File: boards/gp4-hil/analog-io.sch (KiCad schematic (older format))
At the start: 155 parts, among them U10 AD9609, U11 DAC084S085, U12 DAC084S085, U13 DAC084S085, U14 DAC084S085, U19 TS3A4751, U2 XC7A100T-1FTG256C, U25 TS3A4751, U26 TS3A4751, U27 TS3A4751, U28 TS3A4751, U31 ADA4937-2, U34 INA199A2RSW, U35 INA199A2RSW, U36 INA199A2RSW, U8 ADG726, U9 AD9609

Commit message: Began work on footprint creation for layout.
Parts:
- C145, C146, C147, C148, C149, C150, C151, C152, C153, C154, C155, C156, C157, C158, C159, C160, C161, C162, C167, C168, C176, C177, C178, C184, C185, C27, C28, C36, C37, C38, C39, C42, C43, C44, C45, C50, C51, C52, C53: footprint (none) -> azonenberg_pcb:EIA_0402_CAP_NOSILK
- C169, C170, C26, C30, C32, C34, C35, C40, C41, C46, C47, C48, C49, C55: footprint (none) -> azonenberg_pcb:EIA_0603_CAP_NOSILK
- C25, C29, C31, C33, C54, C56: footprint (none) -> azonenberg_pcb:EIA_1206_CAP_NOSILK
- L3, L4, L5: footprint (none) -> azonenberg_pcb:EIA_0805_INDUCTOR_NOSILK

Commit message: Updated PCB with a lot more component footprints
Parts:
- L3, L4, L5: footprint azonenberg_pcb:EIA_0805_INDUCTOR_NOSILK -> azonenberg_pcb:EIA_0603_INDUCTOR_NOSILK
- R138, R139, R140, R141, R59, R60, R61, R62, R63, R64, R65, R66, R67, R68, R69, R70, R71, R72, R73, R74, R75, R76, R77, R78, R79, R80: footprint (none) -> azonenberg_pcb:EIA_0402_RES_NOSILK
- U2: footprint (none) -> azonenberg_pcb:BGA_256_17x17_FULLARRAY_1MM
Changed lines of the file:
@@
 Sheet 5 7
 Title "GreenPak Hardware-In-Loop Test Platform"
-Date "2016-05-19"
+Date "2016-05-20"
 Rev "0.1"
 Comp "Andrew Zonenberg"
@@
 F 0 "U2" H 20850 5850 60  0000 L CNN
 F 1 "XC7A100T-1FTG256C" H 20850 5950 60  0000 L CNN
-F 2 "" H 20850 6050 60  0001 C CNN
+F 2 "azonenberg_pcb:BGA_256_17x17_FULLARRAY_1MM" H 20850 6050 60  0001 C CNN
 F 3 "" H 20850 6050 60  0000 C CNN
 	4    20850 6050
@@
 F 0 "L3" V 8742 750 40  0000 C CNN
 F 1 "600R" V 8820 750 40  0000 C CNN
-F 2 "azonenberg_pcb:EIA_0805_INDUCTOR_NOSILK" H 8900 750 60  0001 C CNN
+F 2 "azonenberg_pcb:EIA_0603_INDUCTOR_NOSILK" H 8900 750 60  0001 C CNN
 F 3 "" H 8900 750 60  0000 C CNN
 	1    8900 750
@@
 F 0 "R60" V 3350 8900 50  0000 C CNN
 F 1 "33" V 3400 8700 50  0000 C CNN
-F 2 "" V 3330 8700 30  0001 C CNN
+F 2 "azonenberg_pcb:EIA_0402_RES_NOSILK" V 3330 8700 30  0001 C CNN
 F 3 "" H 3400 8700 30  0000 C CNN
 	1    3400 8700
@@
 F 0 "R61" V 3350 9000 50  0000 C CNN
 F 1 "33" V 3400 8800 50  0000 C CNN
-F 2 "" V 3330 8800 30  0001 C CNN
+F 2 "azonenberg_pcb:EIA_0402_RES_NOSILK" V 3330 8800 30  0001 C CNN
 F 3 "" H 3400 8800 30  0000 C CNN
 	1    3400 8800
@@
 F 0 "R62" V 3350 9100 50  0000 C CNN
 F 1 "33" V 3400 8900 50  0000 C CNN
-F 2 "" V 3330 8900 30  0001 C CNN
+F 2 "azonenberg_pcb:EIA_0402_RES_NOSILK" V 3330 8900 30  0001 C CNN
 F 3 "" H 3400 8900 30  0000 C CNN
 	1    3400 8900
@@
 F 0 "R63" V 3350 9200 50  0000 C CNN
 F 1 "33" V 3400 9000 50  0000 C CNN
-F 2 "" V 3330 9000 30  0001 C CNN
+F 2 "azonenberg_pcb:EIA_0402_RES_NOSILK" V 3330 9000 30  0001 C CNN
 F 3 "" H 3400 9000 30  0000 C CNN
 	1    3400 9000
@@
 F 0 "R64" V 3350 9300 50  0000 C CNN
 F 1 "33" V 3400 9100 50  0000 C CNN
-F 2 "" V 3330 9100 30  0001 C CNN
+F 2 "azonenberg_pcb:EIA_0402_RES_NOSILK" V 3330 9100 30  0001 C CNN
 F 3 "" H 3400 9100 30  0000 C CNN
 	1    3400 9100
@@
 F 0 "R65" V 3350 9400 50  0000 C CNN
 F 1 "33" V 3400 9200 50  0000 C CNN
-F 2 "" V 3330 9200 30  0001 C CNN
+F 2 "azonenberg_pcb:EIA_0402_RES_NOSILK" V 3330 9200 30  0001 C CNN
 F 3 "" H 3400 9200 30  0000 C CNN
 	1    3400 9200
@@
 F 0 "R66" V 3350 9500 50  0000 C CNN
 F 1 "33" V 3400 9300 50  0000 C CNN
-F 2 "" V 3330 9300 30  0001 C CNN
+F 2 "azonenberg_pcb:EIA_0402_RES_NOSILK" V 3330 9300 30  0001 C CNN
 F 3 "" H 3400 9300 30  0000 C CNN
 	1    3400 9300
@@
 F 0 "R67" V 3350 9600 50  0000 C CNN
 F 1 "33" V 3400 9400 50  0000 C CNN
-F 2 "" V 3330 9400 30  0001 C CNN
+F 2 "azonenberg_pcb:EIA_0402_RES_NOSILK" V 3330 9400 30  0001 C CNN
 F 3 "" H 3400 9400 30  0000 C CNN
 	1    3400 9400
@@
 F 0 "R68" V 3350 9700 50  0000 C CNN
 F 1 "33" V 3400 9500 50  0000 C CNN
-F 2 "" V 3330 9500 30  0001 C CNN
+F 2 "azonenberg_pcb:EIA_0402_RES_NOSILK" V 3330 9500 30  0001 C CNN
 F 3 "" H 3400 9500 30  0000 C CNN
 	1    3400 9500
@@
 F 0 "R69" V 3350 9800 50  0000 C CNN
 F 1 "33" V 3400 9600 50  0000 C CNN
-F 2 "" V 3330 9600 30  0001 C CNN
+F 2 "azonenberg_pcb:EIA_0402_RES_NOSILK" V 3330 9600 30  0001 C CNN
 F 3 "" H 3400 9600 30  0000 C CNN
 	1    3400 9600
@@
 F 0 "R59" V 3350 8700 50  0000 C CNN
 F 1 "33" V 3400 8500 50  0000 C CNN
-F 2 "" V 3330 8500 30  0001 C CNN
+F 2 "azonenberg_pcb:EIA_0402_RES_NOSILK" V 3330 8500 30  0001 C CNN
 F 3 "" H 3400 8500 30  0000 C CNN
 	1    3400 8500
@@
 F 0 "L4" V 6342 750 40  0000 C CNN
 F 1 "600R" V 6420 750 40  0000 C CNN
-F 2 "azonenberg_pcb:EIA_0805_INDUCTOR_NOSILK" H 6500 750 60  0001 C CNN
+F 2 "azonenberg_pcb:EIA_0603_INDUCTOR_NOSILK" H 6500 750 60  0001 C CNN
 F 3 "" H 6500 750 60  0000 C CNN
 	1    6500 750
@@
 F 0 "R71" V 3350 12750 50  0000 C CNN
 F 1 "33" V 3400 12550 50  0000 C CNN
-F 2 "" V 3330 12550 30  0001 C CNN
+F 2 "azonenberg_pcb:EIA_0402_RES_NOSILK" V 3330 12550 30  0001 C CNN
 F 3 "" H 3400 12550 30  0000 C CNN
 	1    3400 12550
@@
 F 0 "R72" V 3350 12850 50  0000 C CNN
 F 1 "33" V 3400 12650 50  0000 C CNN
-F 2 "" V 3330 12650 30  0001 C CNN
+F 2 "azonenberg_pcb:EIA_0402_RES_NOSILK" V 3330 12650 30  0001 C CNN
 F 3 "" H 3400 12650 30  0000 C CNN
 	1    3400 12650
@@
 F 0 "R73" V 3350 12950 50  0000 C CNN
 F 1 "33" V 3400 12750 50  0000 C CNN
-F 2 "" V 3330 12750 30  0001 C CNN
+F 2 "azonenberg_pcb:EIA_0402_RES_NOSILK" V 3330 12750 30  0001 C CNN
 F 3 "" H 3400 12750 30  0000 C CNN
 	1    3400 12750
@@
 F 0 "R74" V 3350 13050 50  0000 C CNN
 F 1 "33" V 3400 12850 50  0000 C CNN
-F 2 "" V 3330 12850 30  0001 C CNN
+F 2 "azonenberg_pcb:EIA_0402_RES_NOSILK" V 3330 12850 30  0001 C CNN
 F 3 "" H 3400 12850 30  0000 C CNN
 	1    3400 12850
@@
 F 0 "R75" V 3350 13150 50  0000 C CNN
 F 1 "33" V 3400 12950 50  0000 C CNN
-F 2 "" V 3330 12950 30  0001 C CNN
+F 2 "azonenberg_pcb:EIA_0402_RES_NOSILK" V 3330 12950 30  0001 C CNN
 F 3 "" H 3400 12950 30  0000 C CNN
 	1    3400 12950
@@
 F 0 "R76" V 3350 13250 50  0000 C CNN
 F 1 "33" V 3400 13050 50  0000 C CNN
-F 2 "" V 3330 13050 30  0001 C CNN
+F 2 "azonenberg_pcb:EIA_0402_RES_NOSILK" V 3330 13050 30  0001 C CNN
 F 3 "" H 3400 13050 30  0000 C CNN
 	1    3400 13050
@@
 F 0 "R77" V 3350 13350 50  0000 C CNN
 F 1 "33" V 3400 13150 50  0000 C CNN
-F 2 "" V 3330 13150 30  0001 C CNN
+F 2 "azonenberg_pcb:EIA_0402_RES_NOSILK" V 3330 13150 30  0001 C CNN
 F 3 "" H 3400 13150 30  0000 C CNN
 	1    3400 13150
@@
 F 0 "R78" V 3350 13450 50  0000 C CNN
 F 1 "33" V 3400 13250 50  0000 C CNN
-F 2 "" V 3330 13250 30  0001 C CNN
+F 2 "azonenberg_pcb:EIA_0402_RES_NOSILK" V 3330 13250 30  0001 C CNN
 F 3 "" H 3400 13250 30  0000 C CNN
 	1    3400 13250
@@
 F 0 "R79" V 3350 13550 50  0000 C CNN
 F 1 "33" V 3400 13350 50  0000 C CNN
-F 2 "" V 3330 13350 30  0001 C CNN
+F 2 "azonenberg_pcb:EIA_0402_RES_NOSILK" V 3330 13350 30  0001 C CNN
 F 3 "" H 3400 13350 30  0000 C CNN
 	1    3400 13350
@@
 F 0 "R80" V 3350 13650 50  0000 C CNN
 F 1 "33" V 3400 13450 50  0000 C CNN
-F 2 "" V 3330 13450 30  0001 C CNN
+F 2 "azonenberg_pcb:EIA_0402_RES_NOSILK" V 3330 13450 30  0001 C CNN
 F 3 "" H 3400 13450 30  0000 C CNN
 	1    3400 13450
@@
 F 0 "R70" V 3350 12550 50  0000 C CNN
 F 1 "33" V 3400 12350 50  0000 C CNN
-F 2 "" V 3330 12350 30  0001 C CNN
+F 2 "azonenberg_pcb:EIA_0402_RES_NOSILK" V 3330 12350 30  0001 C CNN
 F 3 "" H 3400 12350 30  0000 C CNN
 	1    3400 12350
@@
 F 0 "L5" V 6342 1450 40  0000 C CNN
 F 1 "600R" V 6420 1450 40  0000 C CNN
-F 2 "azonenberg_pcb:EIA_0805_INDUCTOR_NOSILK" H 6500 1450 60  0001 C CNN
+F 2 "azonenberg_pcb:EIA_0603_INDUCTOR_NOSILK" H 6500 1450 60  0001 C CNN
 F 3 "" H 6500 1450 60  0000 C CNN
 	1    6500 1450
@@
 F 0 "R140" H 19370 3146 50  0000 L CNN
 F 1 "100" H 19370 3054 50  0000 L CNN
-F 2 "" V 19230 3100 30  0001 C CNN
+F 2 "azonenberg_pcb:EIA_0402_RES_NOSILK" V 19230 3100 30  0001 C CNN
 F 3 "" H 19300 3100 30  0000 C CNN
 	1    19300 3100
@@
 F 0 "R141" H 19370 4946 50  0000 L CNN
 F 1 "100" H 19370 4854 50  0000 L CNN
-F 2 "" V 19230 4900 30  0001 C CNN
+F 2 "azonenberg_pcb:EIA_0402_RES_NOSILK" V 19230 4900 30  0001 C CNN
 F 3 "" H 19300 4900 30  0000 C CNN
 	1    19300 4900
@@
 F 0 "R138" V 1250 9800 50  0000 C CNN
 F 1 "10K 1%" V 1250 9350 50  0000 C CNN
-F 2 "" V 1230 9600 30  0001 C CNN
+F 2 "azonenberg_pcb:EIA_0402_RES_NOSILK" V 1230 9600 30  0001 C CNN
 F 3 "" H 1300 9600 30  0000 C CNN
 	1    1300 9600
@@
 F 0 "R139" V 1250 13650 50  0000 C CNN
 F 1 "10K 1%" V 1250 13200 50  0000 C CNN
-F 2 "" V 1230 13450 30  0001 C CNN
+F 2 "azonenberg_pcb:EIA_0402_RES_NOSILK" V 1230 13450 30  0001 C CNN
 F 3 "" H 1300 13450 30  0000 C CNN
 	1    1300 13450

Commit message: More footprint assignments
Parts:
- R142, R143, R144, R145, R146, R147, R148, R149, R17, R18, R19, R20, R21, R22, R23, R24, R25, R26, R27, R28, R29, R30, R31, R32, R33, R34, R35, R36, R37, R38, R39, R40, R41, R42, R43, R44, R45, R46, R47, R48, R49, R50, R51, R52, R53, R54, R55, R56, R57, R58: footprint (none) -> azonenberg_pcb:EIA_0402_RES_NOSILK
- U19, U25, U26, U27, U28: footprint (none) -> azonenberg_pcb:QFN_14_0.4MM_2x2MM_TI_RUC

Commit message: Finished component footprints. Ready to begin layout.
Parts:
- U10, U9: footprint (none) -> azonenberg_pcb:QFN_32_0.5MM_5x5MM
- U11, U12, U13, U14: footprint (none) -> azonenberg_pcb:DFN_10_0.5MM_3x3MM
- U31: footprint (none) -> azonenberg_pcb:QFN_24_0.5MM_4x4MM
- U34, U35, U36: footprint (none) -> azonenberg_pcb:QFN_10_0.4MM_1.8x1.5MM
- U8: footprint (none) -> azonenberg_pcb:QFN_48_0.5MM_7x7MM
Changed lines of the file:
@@
 Sheet 5 7
 Title "GreenPak Hardware-In-Loop Test Platform"
-Date "2016-05-20"
+Date "2016-05-22"
 Rev "0.1"
 Comp "Andrew Zonenberg"
@@
 F 0 "U8" H 1900 6950 60  0000 C CNN
 F 1 "ADG726" H 2650 6950 60  0000 C CNN
-F 2 "" H 1850 6950 60  0001 C CNN
+F 2 "azonenberg_pcb:QFN_48_0.5MM_7x7MM" H 1850 6950 60  0001 C CNN
 F 3 "" H 1850 6950 60  0000 C CNN
 	1    1850 7000
@@
 F 0 "U9" H 2350 13453 60  0000 C CNN
 F 1 "AD9609" H 2350 13347 60  0000 C CNN
-F 2 "" H 1850 10850 60  0001 C CNN
+F 2 "azonenberg_pcb:QFN_32_0.5MM_5x5MM" H 1850 10850 60  0001 C CNN
 F 3 "" H 1850 10850 60  0000 C CNN
 	1    1850 10850
@@
 F 0 "U10" H 2350 17303 60  0000 C CNN
 F 1 "AD9609" H 2350 17197 60  0000 C CNN
-F 2 "" H 1850 14700 60  0001 C CNN
+F 2 "azonenberg_pcb:QFN_32_0.5MM_5x5MM" H 1850 14700 60  0001 C CNN
 F 3 "" H 1850 14700 60  0000 C CNN
 	1    1850 14700
@@
 F 0 "U11" H 7025 5703 60  0000 C CNN
 F 1 "DAC084S085" H 7025 5597 60  0000 C CNN
-F 2 "" H 6600 4600 60  0001 C CNN
+F 2 "azonenberg_pcb:DFN_10_0.5MM_3x3MM" H 6600 4600 60  0001 C CNN
 F 3 "" H 6600 4600 60  0000 C CNN
 	1    6600 4600
@@
 F 0 "U12" H 7025 6953 60  0000 C CNN
 F 1 "DAC084S085" H 7025 6847 60  0000 C CNN
-F 2 "" H 6600 5850 60  0001 C CNN
+F 2 "azonenberg_pcb:DFN_10_0.5MM_3x3MM" H 6600 5850 60  0001 C CNN
 F 3 "" H 6600 5850 60  0000 C CNN
 	1    6600 5850
@@
 F 0 "U13" H 7025 8203 60  0000 C CNN
 F 1 "DAC084S085" H 7025 8097 60  0000 C CNN
-F 2 "" H 6600 7100 60  0001 C CNN
+F 2 "azonenberg_pcb:DFN_10_0.5MM_3x3MM" H 6600 7100 60  0001 C CNN
 F 3 "" H 6600 7100 60  0000 C CNN
 	1    6600 7100
@@
 F 0 "U14" H 7025 9453 60  0000 C CNN
 F 1 "DAC084S085" H 7025 9347 60  0000 C CNN
-F 2 "" H 6600 8350 60  0001 C CNN
+F 2 "azonenberg_pcb:DFN_10_0.5MM_3x3MM" H 6600 8350 60  0001 C CNN
 F 3 "" H 6600 8350 60  0000 C CNN
 	1    6600 8350
@@
 F 0 "U31" H 11200 13100 60  0000 L CNN
 F 1 "ADA4937-2" H 12200 13100 60  0000 R CNN
-F 2 "" H 11200 13150 60  0001 C CNN
+F 2 "azonenberg_pcb:QFN_24_0.5MM_4x4MM" H 11200 13150 60  0001 C CNN
 F 3 "" H 11200 13150 60  0000 C CNN
 	1    11200 13150
@@
 F 0 "U31" H 11200 14850 60  0000 L CNN
 F 1 "ADA4937-2" H 12200 14850 60  0000 R CNN
-F 2 "" H 11200 14900 60  0001 C CNN
+F 2 "azonenberg_pcb:QFN_24_0.5MM_4x4MM" H 11200 14900 60  0001 C CNN
 F 3 "" H 11200 14900 60  0000 C CNN
 	2    11200 14900
@@
 F 0 "U34" H 17750 9550 60  0000 L CNN
 F 1 "INA199A2RSW" H 18550 9550 60  0000 R CNN
-F 2 "" H 17750 9600 60  0001 C CNN
+F 2 "azonenberg_pcb:QFN_10_0.4MM_1.8x1.5MM" H 17750 9600 60  0001 C CNN
 F 3 "" H 17750 9600 60  0000 C CNN
 	1    17750 9600
@@
 F 0 "U35" H 17750 10750 60  0000 L CNN
 F 1 "INA199A2RSW" H 18550 10750 60  0000 R CNN
-F 2 "" H 17750 10800 60  0001 C CNN
+F 2 "azonenberg_pcb:QFN_10_0.4MM_1.8x1.5MM" H 17750 10800 60  0001 C CNN
 F 3 "" H 17750 10800 60  0000 C CNN
 	1    17750 10800
@@
 F 0 "U36" H 17750 11900 60  0000 L CNN
 F 1 "INA199A2RSW" H 18550 11900 60  0000 R CNN
-F 2 "" H 17750 11950 60  0001 C CNN
+F 2 "azonenberg_pcb:QFN_10_0.4MM_1.8x1.5MM" H 17750 11950 60  0001 C CNN
 F 3 "" H 17750 11950 60  0000 C CNN
 	1    17750 11950

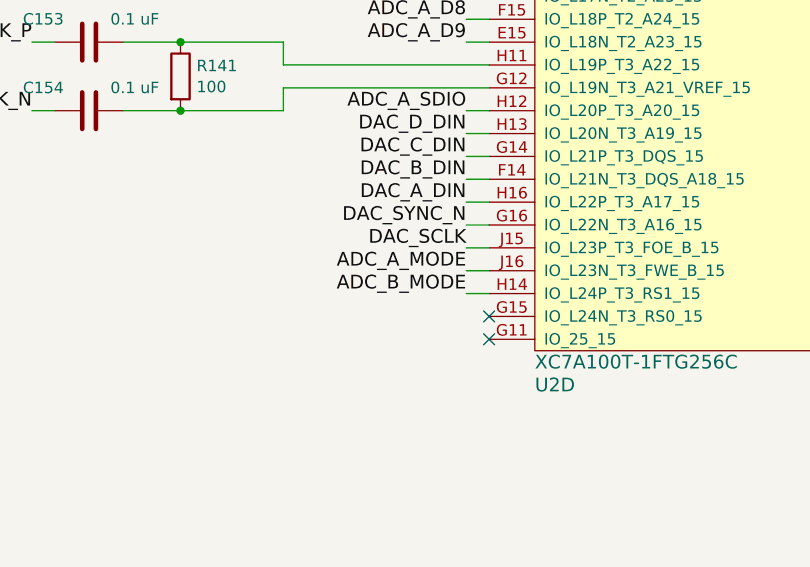
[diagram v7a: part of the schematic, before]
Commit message: Began routing level shifters
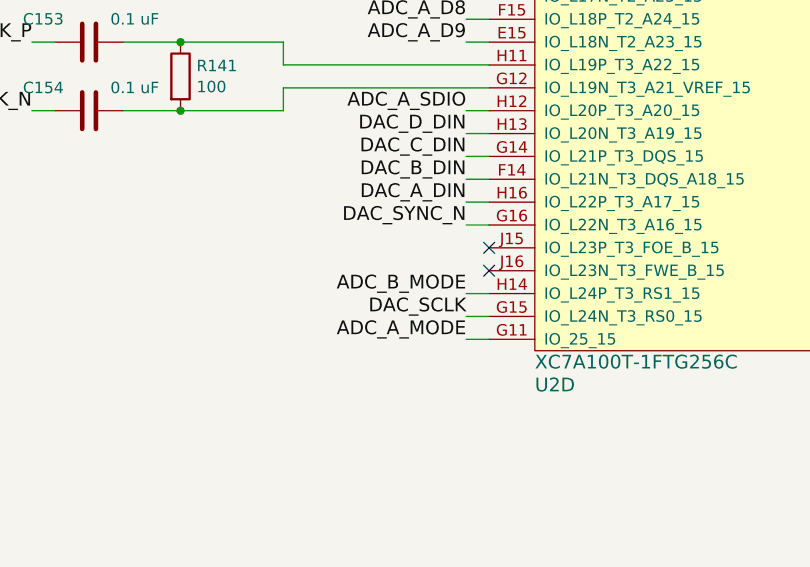
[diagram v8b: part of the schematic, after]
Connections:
- net ADC_A_MODE: now also U2.G11 (IO_25_15); no longer U2.J16 (IO_L23N_T3_FWE_B_15)
- net DAC_SCLK: now also U2.G15 (IO_L24N_T3_RS0_15); no longer U2.J15 (IO_L23P_T3_FOE_B_15)
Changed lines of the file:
@@
 Sheet 5 7
 Title "GreenPak Hardware-In-Loop Test Platform"
-Date "2016-05-26"
+Date "2016-05-28"
 Rev "0.1"
 Comp "Andrew Zonenberg"
@@
 Text Label 20550 5150 2    60   ~ 0
 DAC_D_DIN
-Text Label 20550 5650 2    60   ~ 0
+Text Label 20550 5950 2    60   ~ 0
 DAC_SCLK
-NoConn ~ 20650 5950
-NoConn ~ 20650 6050
 $Comp
 L AD9609 U10
@@
 	20650 5550 20550 5550
 Wire Wire Line
-	20550 5650 20650 5650
+	20550 5950 20650 5950
 Wire Wire Line
 	3050 12550 3250 12550
@@
 Text Label 20550 5850 2    60   ~ 0
 ADC_B_MODE
-Text Label 20550 5750 2    60   ~ 0
+Text Label 20550 6050 2    60   ~ 0
 ADC_A_MODE
 Wire Wire Line
-	20550 5750 20650 5750
+	20550 6050 20650 6050
 Wire Wire Line
 	20650 5850 20550 5850
@@
 Text Label 5500 1750 2    60   ~ 0
 GND
+NoConn ~ 20650 5650
+NoConn ~ 20650 5750
 $EndSCHEMATC
